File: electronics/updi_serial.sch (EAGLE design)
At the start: 11 parts, among them U1 CH340N

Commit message: changed pin hdr package, updated silk
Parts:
- JP1: device pinhead-2:PINHD-1X03_2.54-90°-S -> pinhead-2:PINHD-1X03_2.54-S
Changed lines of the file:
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@@
 <grid distance="0.1" unitdist="inch" unit="inch" style="lines" multiple="1" display="no" altdistance="0.01" altunitdist="inch" altunit="inch"/>
 <layers>
-<layer number="1" name="Top" color="4" fill="1" visible="no" active="no"/>
-<layer number="16" name="Bottom" color="1" fill="1" visible="no" active="no"/>
-<layer number="17" name="Pads" color="2" fill="1" visible="no" active="no"/>
-<layer number="18" name="Vias" color="2" fill="1" visible="no" active="no"/>
-<layer number="19" name="Unrouted" color="6" fill="1" visible="no" active="no"/>
-<layer number="20" name="Dimension" color="15" fill="1" visible="no" active="no"/>
-<layer number="21" name="tPlace" color="7" fill="1" visible="no" active="no"/>
-<layer number="22" name="bPlace" color="7" fill="1" visible="no" active="no"/>
-<layer number="23" name="tOrigins" color="15" fill="1" visible="no" active="no"/>
-<layer number="24" name="bOrigins" color="15" fill="1" visible="no" active="no"/>
-<layer number="25" name="tNames" color="7" fill="1" visible="no" active="no"/>
-<layer number="26" name="bNames" color="7" fill="1" visible="no" active="no"/>
-<layer number="27" name="tValues" color="7" fill="1" visible="no" active="no"/>
-<layer number="28" name="bValues" color="7" fill="1" visible="no" active="no"/>
+<layer number="1" name="Top" color="4" fill="1" visible="yes" active="no"/>
+<layer number="16" name="Bottom" color="1" fill="1" visible="yes" active="no"/>
+<layer number="17" name="Pads" color="2" fill="1" visible="yes" active="no"/>
+<layer number="18" name="Vias" color="2" fill="1" visible="yes" active="no"/>
+<layer number="19" name="Unrouted" color="6" fill="1" visible="yes" active="no"/>
+<layer number="20" name="Dimension" color="15" fill="1" visible="yes" active="no"/>
+<layer number="21" name="tPlace" color="7" fill="1" visible="yes" active="no"/>
+<layer number="22" name="bPlace" color="7" fill="1" visible="yes" active="no"/>
+<layer number="23" name="tOrigins" color="15" fill="1" visible="yes" active="no"/>
+<layer number="24" name="bOrigins" color="15" fill="1" visible="yes" active="no"/>
+<layer number="25" name="tNames" color="7" fill="1" visible="yes" active="no"/>
+<layer number="26" name="bNames" color="7" fill="1" visible="yes" active="no"/>
+<layer number="27" name="tValues" color="7" fill="1" visible="yes" active="no"/>
+<layer number="28" name="bValues" color="7" fill="1" visible="yes" active="no"/>
 <layer number="29" name="tStop" color="7" fill="3" visible="no" active="no"/>
 <layer number="30" name="bStop" color="7" fill="6" visible="no" active="no"/>
@@
 <layer number="35" name="tGlue" color="7" fill="4" visible="no" active="no"/>
 <layer number="36" name="bGlue" color="7" fill="5" visible="no" active="no"/>
-<layer number="37" name="tTest" color="7" fill="1" visible="no" active="no"/>
-<layer number="38" name="bTest" color="7" fill="1" visible="no" active="no"/>
+<layer number="37" name="tTest" color="7" fill="1" visible="yes" active="no"/>
+<layer number="38" name="bTest" color="7" fill="1" visible="yes" active="no"/>
 <layer number="39" name="tKeepout" color="4" fill="11" visible="no" active="no"/>
 <layer number="40" name="bKeepout" color="1" fill="11" visible="no" active="no"/>
@@
 <layer number="44" name="Drills" color="7" fill="1" visible="no" active="no"/>
 <layer number="45" name="Holes" color="7" fill="1" visible="no" active="no"/>
-<layer number="46" name="Milling" color="3" fill="1" visible="no" active="no"/>
-<layer number="47" name="Measures" color="7" fill="1" visible="no" active="no"/>
-<layer number="48" name="Document" color="7" fill="1" visible="no" active="no"/>
-<layer number="49" name="Reference" color="7" fill="1" visible="no" active="no"/>
-<layer number="50" name="dxf" color="7" fill="1" visible="no" active="no"/>
-<layer number="51" name="tDocu" color="7" fill="1" visible="no" active="no"/>
-<layer number="52" name="bDocu" color="7" fill="1" visible="no" active="no"/>
-<layer number="53" name="tGND_GNDA" color="7" fill="9" visible="no" active="no"/>
-<layer number="54" name="bGND_GNDA" color="1" fill="9" visible="no" active="no"/>
-<layer number="56" name="wert" color="7" fill="1" visible="no" active="no"/>
-<layer number="57" name="tCAD" color="7" fill="1" visible="no" active="no"/>
-<layer number="59" name="tCarbon" color="7" fill="1" visible="no" active="no"/>
-<layer number="60" name="bCarbon" color="7" fill="1" visible="no" active="no"/>
+<layer number="46" name="Milling" color="3" fill="1" visible="yes" active="no"/>
+<layer number="47" name="Measures" color="7" fill="1" visible="yes" active="no"/>
+<layer number="48" name="Document" color="7" fill="1" visible="yes" active="no"/>
+<layer number="49" name="Reference" color="7" fill="1" visible="yes" active="no"/>
+<layer number="50" name="dxf" color="7" fill="1" visible="yes" active="no"/>
+<layer number="51" name="tDocu" color="7" fill="1" visible="yes" active="no"/>
+<layer number="52" name="bDocu" color="7" fill="1" visible="yes" active="no"/>
+<layer number="53" name="tGND_GNDA" color="7" fill="9" visible="yes" active="no"/>
+<layer number="54" name="bGND_GNDA" color="1" fill="9" visible="yes" active="no"/>
+<layer number="56" name="wert" color="7" fill="1" visible="yes" active="no"/>
+<layer number="57" name="tCAD" color="7" fill="1" visible="yes" active="no"/>
+<layer number="59" name="tCarbon" color="7" fill="1" visible="yes" active="no"/>
+<layer number="60" name="bCarbon" color="7" fill="1" visible="yes" active="no"/>
 <layer number="90" name="Modules" color="5" fill="1" visible="yes" active="yes"/>
 <layer number="91" name="Nets" color="2" fill="1" visible="yes" active="yes"/>
@@
 </classes>
 <parts>
-<part name="JP1" library="pinhead-2" deviceset="PINHD-1X03" device="_2.54-90°-S"/>
+<part name="JP1" library="pinhead-2" deviceset="PINHD-1X03" device="_2.54-S"/>
 <part name="JP2" library="bt_electromech" deviceset="USB" device="-MINIB"/>
 <part name="LED1" library="bt_opto" deviceset="LED" device="CHIPLED_1206" value="PWR"/>

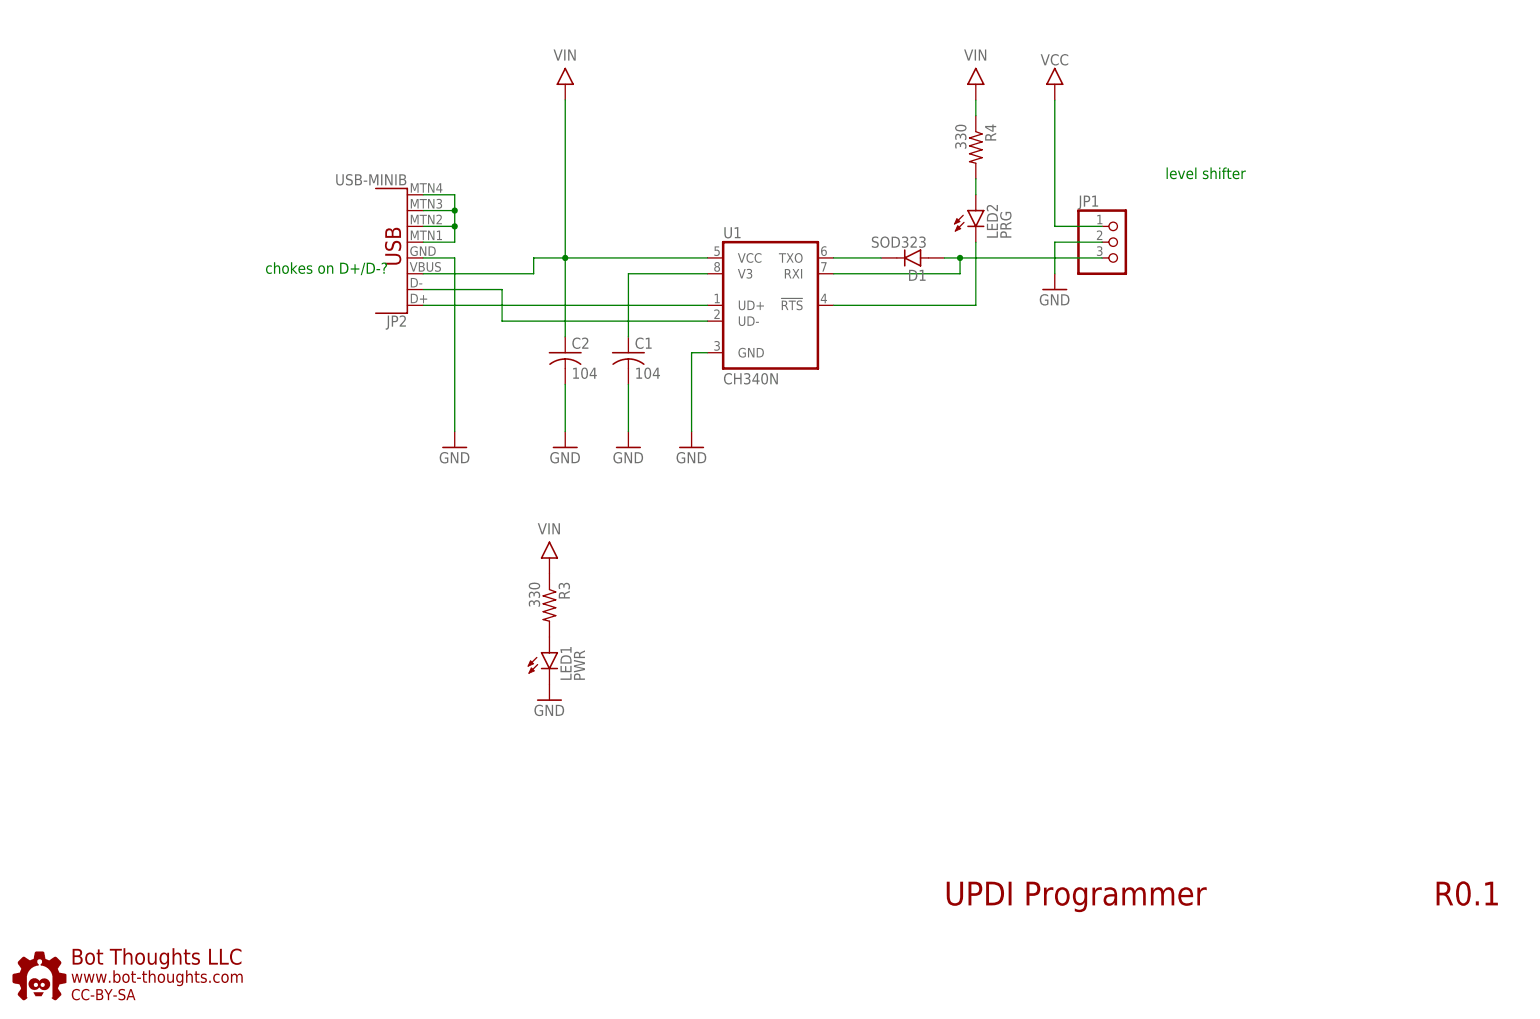
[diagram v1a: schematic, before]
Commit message: replaced solder jmpr with pin hdr, layout changes, pwr led indicates target pwr now
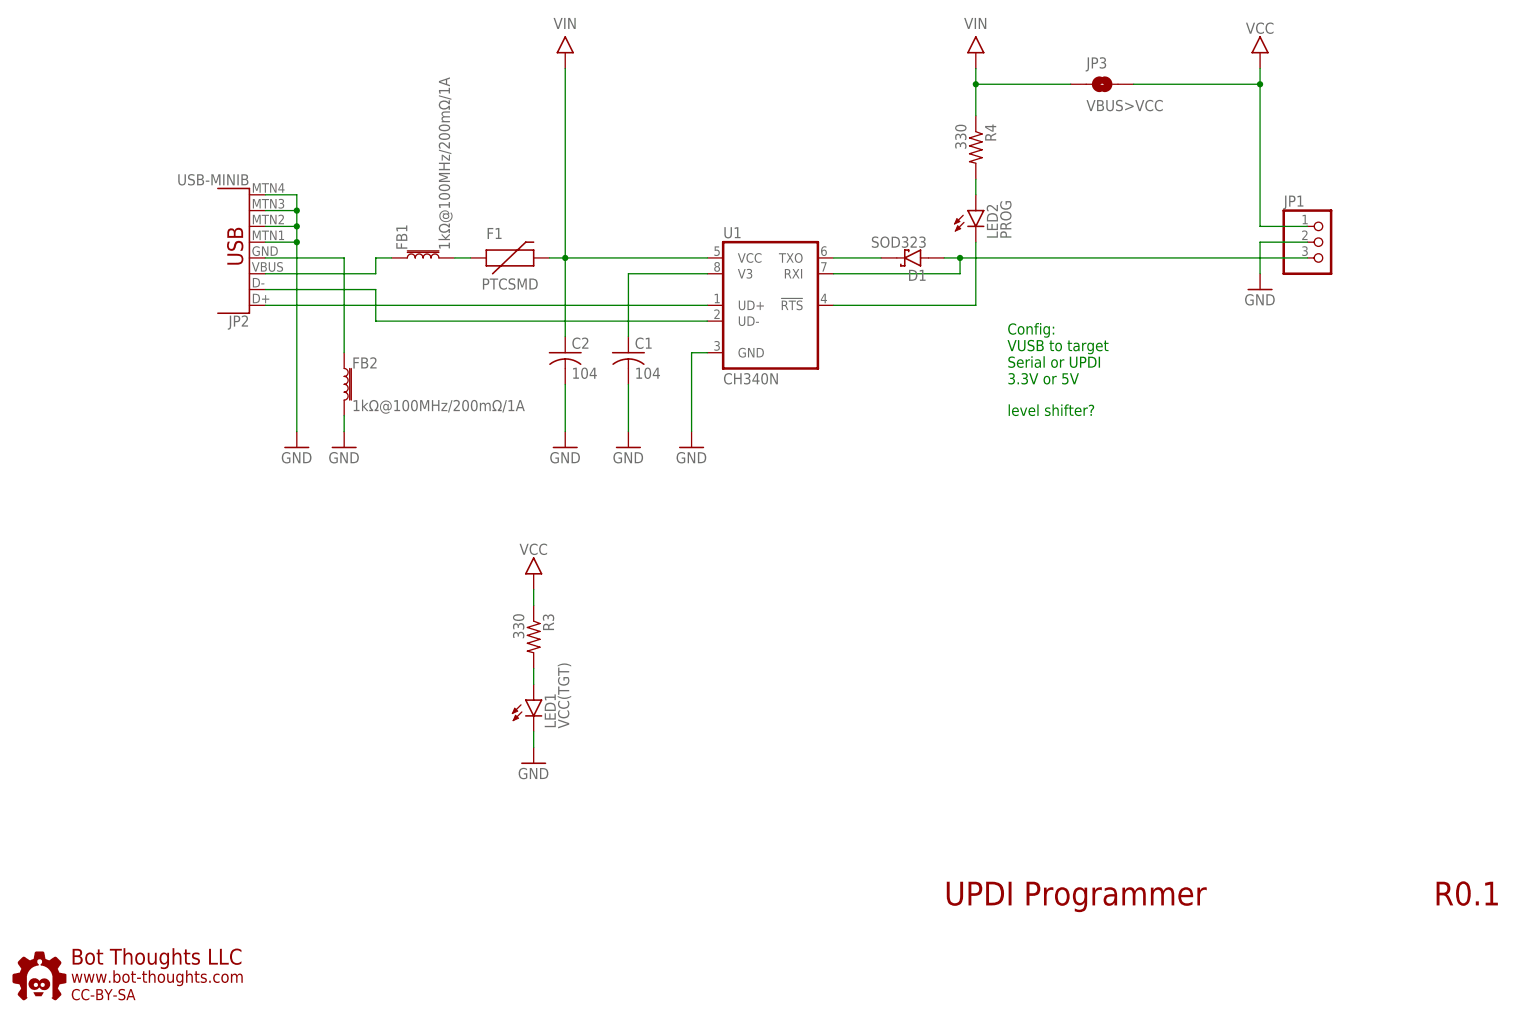
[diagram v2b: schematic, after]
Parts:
- added F1: PTCSMD, bt:PTCSMD
- added FB1, FB2: 1kΩ@100MHz/200mΩ/1A, SparkFun-Coils:FERRITE_BEAD-0603
- added JP3: VBUS>VCC, bt:JUMPER-PTH-0.1IN
- D1: device bt_diode:DIODE_SOD323 -> bt_diode:SCHOTTKY-DIODE-MBR130LSFT1
- LED1: value PWR -> VCC(TGT)
- LED2: value PRG -> PROG
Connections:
- removed net SHIELD: JP2.SHIELD1, JP2.SHIELD2, JP2.SHIELD3, JP2.SHIELD4
- new net N$1: FB1.1, JP2.VBUS
- new net N$2: F1.1, FB1.2
- new net N$7: FB2.1, JP2.GND
- net GND: now also FB2.2, JP2.SHIELD1, JP2.SHIELD2, JP2.SHIELD3, JP2.SHIELD4; no longer JP2.GND
- net VCC: now also JP3.2, R3.1
- net VIN: now also F1.2, JP3.1; no longer JP2.VBUS, R3.1
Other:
- note added: "Config: VUSB to target Serial or UPDI 3.3V or 5V"
- note added: "level shifter?"
- note removed: "chokes on D+/D-?"
- note removed: "level shifter"
- moved on the sheet: JP1, JP2, LED1, R3
